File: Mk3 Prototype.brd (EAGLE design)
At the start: 113 x 55.2 mm, 176 parts, among them IC1 BD49XXX, IC2 CC3100, IC3 S25FL216K0PMFI011, IC4 STM32F401V, IC6 AP3419, J1 ZX62-AB-5PA(11), J2 SWD_SHROUD, J7 SFV30R-2STE1HLF, Q1 BSS84W, Q11 BSS84W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

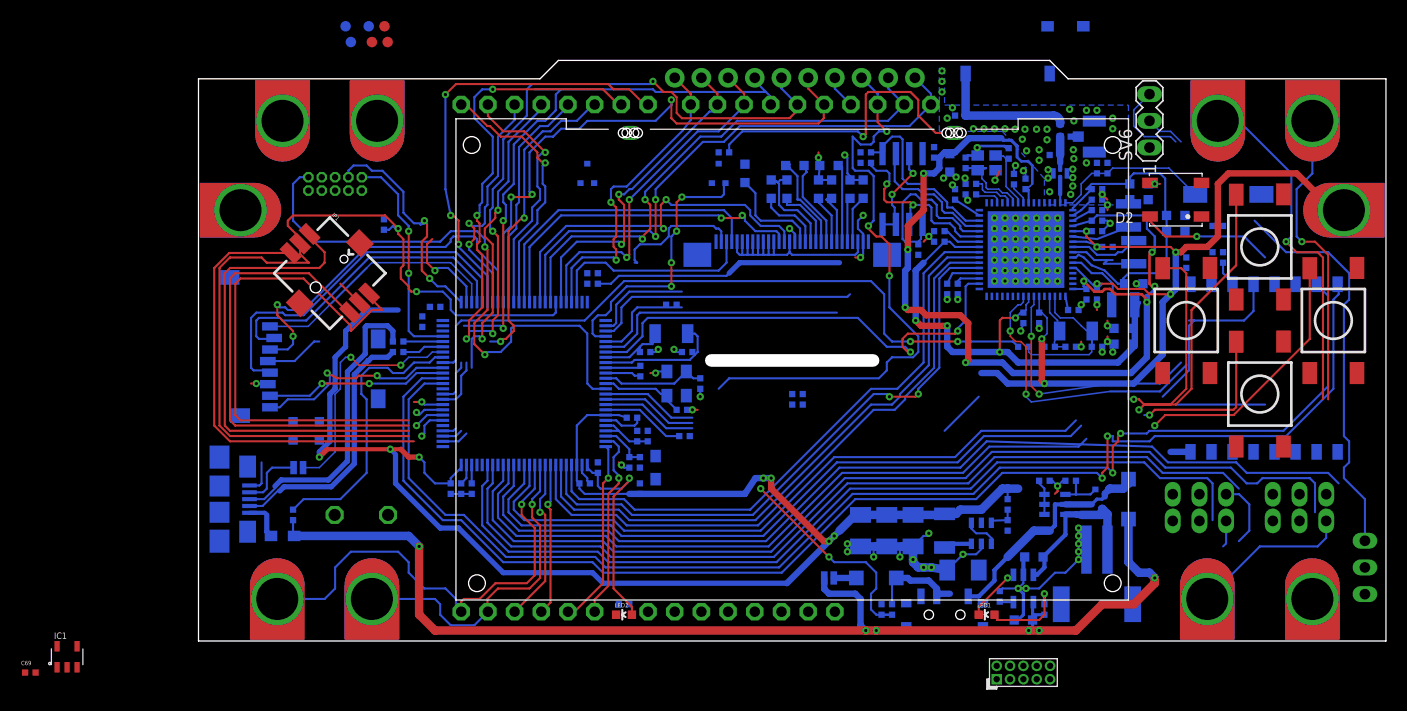
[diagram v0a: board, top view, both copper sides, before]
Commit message: added notes, increased via size
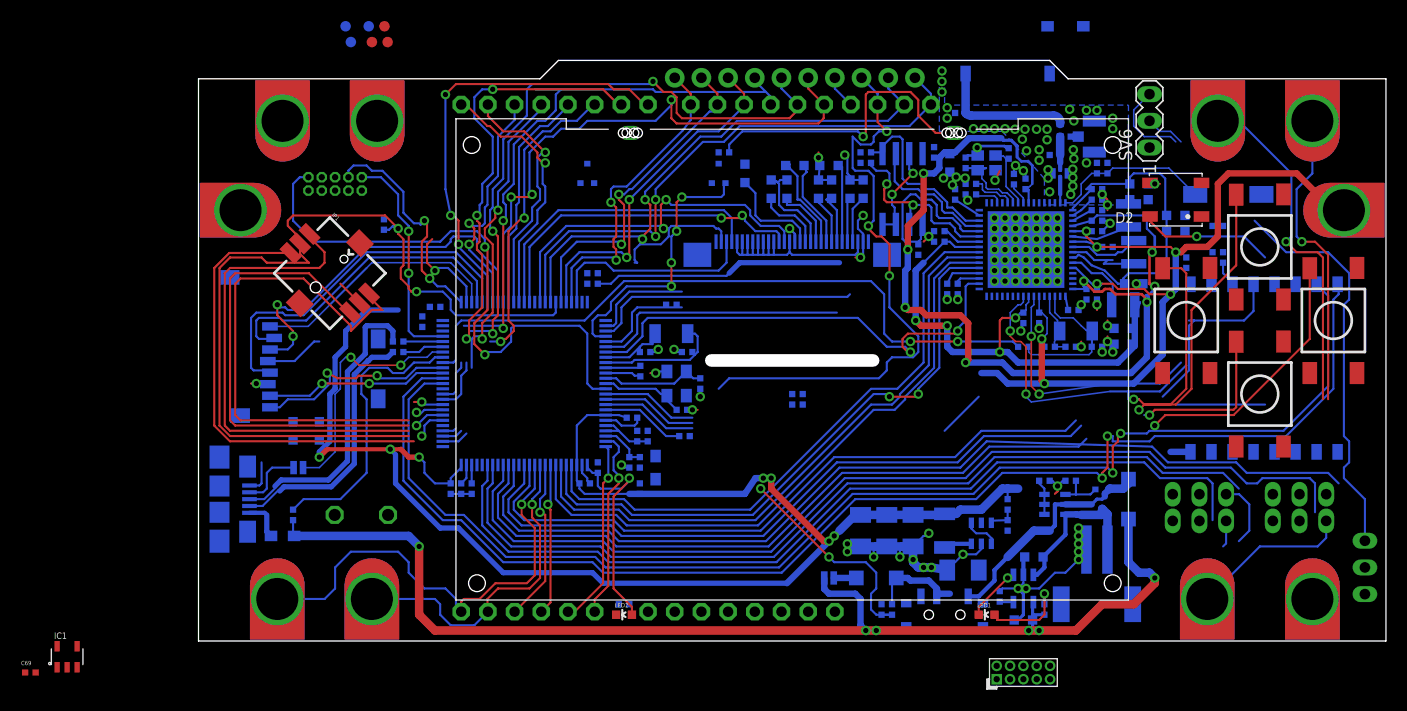
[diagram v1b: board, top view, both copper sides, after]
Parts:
- moved C2 0.25 mm to (72.5, 50.2)

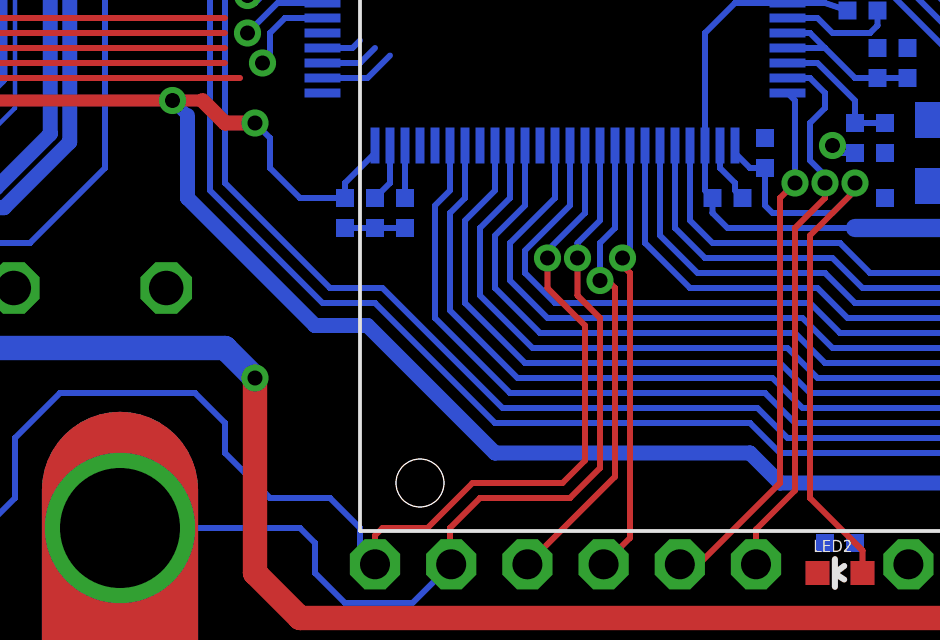
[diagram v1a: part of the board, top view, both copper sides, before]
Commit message: added two status leds
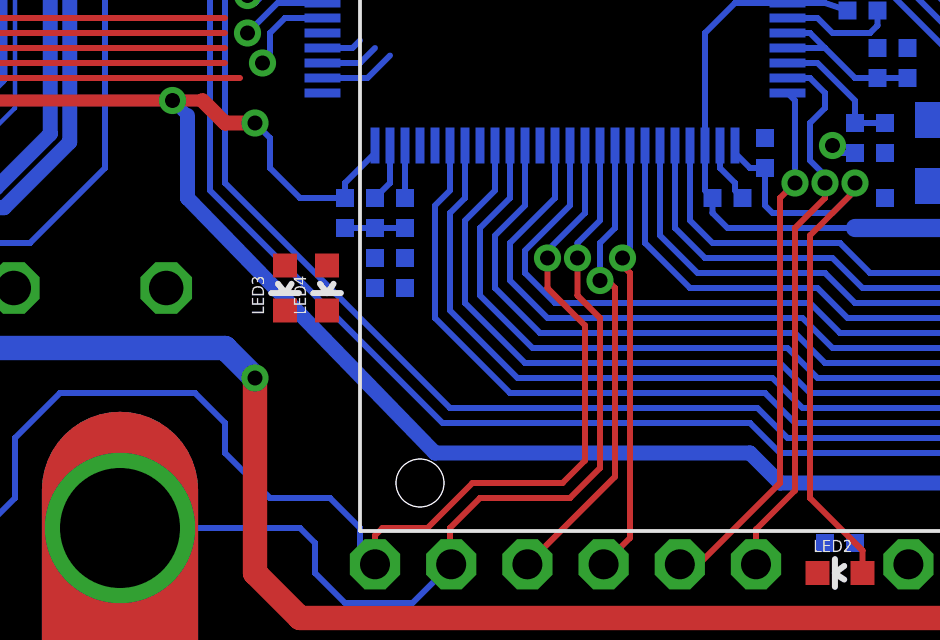
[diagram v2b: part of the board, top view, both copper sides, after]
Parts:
- added LED3, LED4: (no value), TiLDA Mk3 Parts:LED-0603-CORRECT
- added R34, R35: (no value), TiLDA Mk3 Parts:R0402-SMALLER
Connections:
- new net LED1: IC4.46, R34.2
- new net LED2: IC4.47, R35.2
- new net N$51: LED4.A, R35.1
- new net N$52: LED3.A, R34.1
- net GND: now also LED3.C, LED4.C
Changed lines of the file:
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@@
 <setting verticaltext="up"/>
 </settings>
-<grid distance="0.1" unitdist="mm" unit="mm" style="lines" multiple="1" display="yes" altdistance="0.25" altunitdist="mm" altunit="mm"/>
+<grid distance="0.5" unitdist="mm" unit="mm" style="lines" multiple="1" display="yes" altdistance="0.25" altunitdist="mm" altunit="mm"/>
 <layers>
 <layer number="1" name="Top" color="4" fill="1" visible="yes" active="yes"/>
@@
 <element name="IC1" library="TiLDA Mk3 Parts" package="SSOP5" value="BD49XXX" x="-12.5" y="-1.5"/>
 <element name="C69" library="TiLDA Mk3 Parts" package="C0402-SMALLER" value="0402/1n/10V/X5R" x="-16" y="-3"/>
+<element name="LED3" library="TiLDA Mk3 Parts" package="LED-0603-CORRECT" value="" x="22" y="12" rot="R90"/>
+<element name="LED4" library="TiLDA Mk3 Parts" package="LED-0603-CORRECT" value="" x="23.4" y="12" rot="R90"/>
+<element name="R34" library="TiLDA Mk3 Parts" package="R0402-SMALLER" value="" x="25.5" y="12" rot="MR180"/>
+<element name="R35" library="TiLDA Mk3 Parts" package="R0402-SMALLER" value="" x="25.5" y="13" rot="MR180"/>
 </elements>
 <signals>
@@
 <contactref element="IC1" pad="3"/>
 <contactref element="C69" pad="2"/>
+<contactref element="LED4" pad="C"/>
+<contactref element="LED3" pad="C"/>
 <wire x1="82.9" y1="50.6" x2="84.2" y2="58.5" width="0" layer="19" extent="16-16"/>
 <wire x1="81.35" y1="44.5" x2="82.65" y2="44.5" width="0" layer="19" extent="16-16"/>
@@
 <wire x1="56.5" y1="23.5" x2="47.75" y2="23.25" width="0" layer="19" extent="16-16"/>
 <wire x1="26" y1="14" x2="36.5" y2="16" width="0" layer="19" extent="16-16"/>
-<wire x1="18.04" y1="12" x2="24" y2="14" width="0" layer="19" extent="16-16"/>
+<wire x1="23.4" y1="11.25" x2="24" y2="14" width="0" layer="19" extent="1-16"/>
+<wire x1="22" y1="11.25" x2="23.4" y2="11.25" width="0" layer="19" extent="1-1"/>
+<wire x1="18.04" y1="12" x2="22" y2="11.25" width="0" layer="19" extent="1-1"/>
 <wire x1="12.96" y1="12" x2="18.04" y2="12" width="0" layer="19" extent="1-1"/>
 <wire x1="6" y1="15" x2="12.96" y2="12" width="0" layer="19" extent="16-16"/>
@@
 <via x="18.25" y="18.25" extent="1-16" drill="0.5" shape="octagon"/>
 <wire x1="18.75" y1="17.75" x2="18.75" y2="15" width="0.5" layer="16"/>
-<wire x1="18.75" y1="15" x2="23" y2="10.75" width="0.5" layer="16"/>
-<wire x1="23" y1="10.75" x2="24.75" y2="10.75" width="0.5" layer="16"/>
-<wire x1="24.75" y1="10.75" x2="29" y2="6.5" width="0.5" layer="16"/>
-<wire x1="29" y1="6.5" x2="37.5" y2="6.5" width="0.5" layer="16"/>
+<wire x1="18.75" y1="15" x2="27" y2="6.5" width="0.5" layer="16"/>
+<wire x1="27" y1="6.5" x2="37.5" y2="6.5" width="0.5" layer="16"/>
 <wire x1="37.5" y1="6.5" x2="38.5" y2="5.5" width="0.5" layer="16"/>
 <wire x1="38.5" y1="5.5" x2="56" y2="5.5" width="0.5" layer="16"/>
@@
 <wire x1="21.5" y1="24.5" x2="20" y2="23" width="0.2" layer="16"/>
 <wire x1="20" y1="23" x2="20" y2="15.5" width="0.2" layer="16"/>
-<wire x1="20" y1="15.5" x2="23.5" y2="12" width="0.2" layer="16"/>
-<wire x1="23.5" y1="12" x2="25.25" y2="12" width="0.2" layer="16"/>
-<wire x1="25.25" y1="12" x2="29.25" y2="8" width="0.2" layer="16"/>
-<wire x1="29.25" y1="8" x2="37.75" y2="8" width="0.2" layer="16"/>
+<wire x1="20" y1="15.5" x2="27.5" y2="8" width="0.2" layer="16"/>
+<wire x1="27.5" y1="8" x2="37.75" y2="8" width="0.2" layer="16"/>
 <wire x1="37.75" y1="8" x2="38.75" y2="7" width="0.2" layer="16"/>
 <wire x1="38.75" y1="7" x2="55.25" y2="7" width="0.2" layer="16"/>
@@
 <wire x1="21.25" y1="25" x2="19.5" y2="23.25" width="0.2" layer="16"/>
 <wire x1="19.5" y1="23.25" x2="19.5" y2="15.25" width="0.2" layer="16"/>
-<wire x1="19.5" y1="15.25" x2="23.25" y2="11.5" width="0.2" layer="16"/>
-<wire x1="23.25" y1="11.5" x2="25" y2="11.5" width="0.2" layer="16"/>
-<wire x1="25" y1="11.5" x2="29" y2="7.5" width="0.2" layer="16"/>
-<wire x1="29" y1="7.5" x2="37.5" y2="7.5" width="0.2" layer="16"/>
+<wire x1="19.5" y1="15.25" x2="27.25" y2="7.5" width="0.2" layer="16"/>
+<wire x1="27.25" y1="7.5" x2="37.5" y2="7.5" width="0.2" layer="16"/>
 <wire x1="74" y1="13.5" x2="62.5" y2="13.5" width="0.2" layer="16"/>
 <wire x1="62.5" y1="13.5" x2="55.5" y2="6.5" width="0.2" layer="16"/>
@@
 <contactref element="SV1" pad="2"/>
 </signal>
+<signal name="N$51">
+<contactref element="LED4" pad="A"/>
+<contactref element="R35" pad="1"/>
+<wire x1="25" y1="13" x2="23.4" y2="12.75" width="0" layer="19" extent="1-16"/>
+</signal>
+<signal name="N$52">
+<contactref element="LED3" pad="A"/>
+<contactref element="R34" pad="1"/>
+<wire x1="25" y1="12" x2="22" y2="12.75" width="0" layer="19" extent="1-16"/>
+</signal>
+<signal name="LED1">
+<contactref element="R34" pad="2"/>
+<contactref element="IC4" pad="46"/>
+<wire x1="26" y1="12" x2="27" y2="16.75" width="0" layer="19" extent="16-16"/>
+</signal>
+<signal name="LED2">
+<contactref element="R35" pad="2"/>
+<contactref element="IC4" pad="47"/>
+<wire x1="26" y1="13" x2="26.5" y2="16.75" width="0" layer="19" extent="16-16"/>
+</signal>
 </signals>

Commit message: power supply improvments
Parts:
- added D3: (no value), diode:SOD80C
- added F1: PTCSMD, SparkFun-PowerIC:PTC-1206
- added R36: 0402/47k/5%, TiLDA Mk3 Parts:R0402-SMALLER
- C37: value 0603/4u7u/10V/X5R -> 0603/4u7/10V/X5R
- C38: value (none) -> 0603/10u/16V/X5R; device TiLDA Mk3 Parts:C0603K-SMALL -> TiLDA Mk3 Parts:C0805K
- C58: value 22u -> 0603/10u/10V/X5R; device TiLDA Mk3 Parts:C1206K -> TiLDA Mk3 Parts:C0805K
- C59: value 22u -> 0402/4u7/10V/X5R; device TiLDA Mk3 Parts:C1206K -> TiLDA Mk3 Parts:C0402-SMALLER
- C60: value (none) -> 0603/1u/10V/X5R; device TiLDA Mk3 Parts:C1206K -> TiLDA Mk3 Parts:C0402-SMALLER
- C61: value 22u -> 0603/10u/16V/X5R; device TiLDA Mk3 Parts:C1206K -> TiLDA Mk3 Parts:C0805K
- C69: value 0402/1n/10V/X5R -> 0402/1n/10V/NP0
- R17: value (none) -> 0402/2k/5%
- R19, R20, R25, R26: value (none) -> 0402/220k/5%
- R22: value (none) -> 0402/2M2/5%
- moved C69 84.1 mm to (66.8, 12.0), flipped to the bottom, turned to 180 degrees
- moved IC1 76.0 mm to (62.8, 9.50), flipped to the bottom, turned to 180 degrees
- moved C60 21.0 mm to (43.0, 17.0), turned to 90 degrees
- moved R31 12.7 mm to (65.0, 8.75), turned to 90 degrees
- moved R32 12.0 mm to (65.0, 10.5), turned to 90 degrees
- moved C58 10.0 mm to (75.5, 9.50), turned to 90 degrees
- moved IC6 7.02 mm to (67.5, 9.75), turned to 180 degrees
- moved C59 6.26 mm to (62.5, 7.50), turned to 0 degrees
- moved C61 4.07 mm to (70.0, 9.75), turned to 90 degrees
- moved L5 2.92 mm to (46.0, 18.0), turned to 0 degrees
- moved G1 2.85 mm to (17.2, 14.2), turned to 270 degrees
- moved L6 2.00 mm to (8.00, 12.0)
- moved L7 1.80 mm to (72.5, 9.50), turned to 270 degrees
- moved R27 1.25 mm to (9.00, 13.2), turned to 0 degrees
- moved R34 0.79 mm to (26.2, 11.8), turned to 90 degrees
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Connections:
- new net N$55: F1.1, L6.2
- new net N$56: C59.1, IC1.2, R36.2
- net +3V3: no longer C59.1, C60.1
- net ADC_VBUS: now also C60.2
- net GND: now also C60.1, D3.A, U1.CD2; no longer C60.2
- net SDIO_SW: now also U1.CD1
- net VBUS: now also D3.C, F1.2; no longer L6.2
- net V_UNREG: now also R36.1; no longer IC1.2
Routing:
- net +3V3: track 286.0 -> 267.2 mm
- net VBUS: track 114.6 -> 98.3 mm, vias 6 -> 2
- net N$12: track 0.00 -> 6.91 mm
- net N$52: track 0.00 -> 5.02 mm, vias 0 -> 1
- net LED1: track 0.00 -> 4.96 mm
- net V_UNREG: track 12.6 -> 17.6 mm
- net LED2: track 0.00 -> 4.16 mm
- net N$56: track 0.00 -> 4.10 mm
- net N$26: track 2.64 -> 6.08 mm
- net N$55: track 0.00 -> 3.33 mm
- net GND: track 120.1 -> 123.4 mm, vias 138 -> 137
- net N$51: track 0.00 -> 2.52 mm, vias 0 -> 1
- net N$27: track 3.90 -> 2.13 mm
- net ADC_LIGHT: track 20.7 -> 21.9 mm
- net ADC_VIN: track 29.3 -> 30.1 mm
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
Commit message: bit of tidying up
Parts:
- removed D3: (no value), diode:SOD80C
- added R37: 0402/100K/5%, TiLDA Mk3 Parts:R0402-SMALLER
- R12, R13: value 0402/100K/5% -> 0402/220K/5%
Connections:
- net GND: now also R37.1; no longer D3.A
- net MOM_LEFT: now also R37.2
- net VBUS: no longer D3.C
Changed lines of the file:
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@@
 <element name="C32" library="TiLDA Mk3 Parts" package="C0402-SMALLER" value="0402/100n/10V/X5R" x="41.75" y="19.5" rot="MR270"/>
 <element name="C33" library="TiLDA Mk3 Parts" package="C0402-SMALLER" value="0402/100n/10V/X5R" x="42.75" y="19.5" rot="MR270"/>
-<element name="R12" library="TiLDA Mk3 Parts" package="R0402-SMALLER" value="0402/100K/5%" x="57" y="23.5" rot="MR0"/>
-<element name="R13" library="TiLDA Mk3 Parts" package="R0402-SMALLER" value="0402/100K/5%" x="57" y="22.5" rot="MR0"/>
+<element name="R12" library="TiLDA Mk3 Parts" package="R0402-SMALLER" value="0402/220K/5%" x="57" y="23.5" rot="MR0"/>
+<element name="R13" library="TiLDA Mk3 Parts" package="R0402-SMALLER" value="0402/220K/5%" x="57" y="22.5" rot="MR0"/>
 <element name="C34" library="TiLDA Mk3 Parts" package="C0402-SMALLER" value="0402/1u/10V/X5R" x="45" y="32" rot="MR0"/>
 <element name="R14" library="TiLDA Mk3 Parts" package="R0402-SMALLER" value="0402/100K/5%" x="17.646" y="39.636" rot="MR270"/>
@@
 <attribute name="PROD_ID" value="RES-11150" x="8.5" y="9.5" size="1.778" layer="28" rot="MR180" display="off"/>
 </element>
-<element name="D3" library="diode" package="SOD80C" value="" x="11.75" y="10" rot="MR90"/>
 <element name="C59" library="TiLDA Mk3 Parts" package="C0402-SMALLER" value="0402/4u7/10V/X5R" x="62.5" y="7.5" rot="MR0"/>
 <element name="R36" library="TiLDA Mk3 Parts" package="R0402-SMALLER" value="0402/47k/5%" x="64.5" y="7.5" rot="MR0"/>
 <element name="C60" library="TiLDA Mk3 Parts" package="C0402-SMALLER" value="0603/1u/10V/X5R" x="43" y="17" rot="MR90"/>
+<element name="R37" library="TiLDA Mk3 Parts" package="R0402-SMALLER" value="0402/100K/5%" x="-11.5" y="-3"/>
 </elements>
 <signals>
@@
 <wire x1="22.5" y1="12.75" x2="22" y2="12.75" width="0.2" layer="1"/>
 <wire x1="22.5" y1="14.25" x2="22.5" y2="12.75" width="0.2" layer="1"/>
-<contactref element="D3" pad="A"/>
 <contactref element="C59" pad="2"/>
 <contactref element="C60" pad="1"/>
@@
 <wire x1="74.75" y1="11.5" x2="74.75" y2="11.25" width="0.2" layer="16"/>
 <wire x1="74.75" y1="11.25" x2="75.5" y2="10.5" width="0.2" layer="16"/>
+<contactref element="R37" pad="1"/>
 <wire x1="82.9" y1="50.6" x2="84.2" y2="58.5" width="0" layer="19" extent="16-16"/>
 <wire x1="81.35" y1="44.5" x2="82.65" y2="44.5" width="0" layer="19" extent="16-16"/>
@@
 <wire x1="41.75" y1="20" x2="42.75" y2="20" width="0" layer="19" extent="16-16"/>
 <wire x1="41.5" y1="20.5" x2="41.75" y2="20" width="0" layer="19" extent="16-16"/>
-<wire x1="43" y1="16.5" x2="42.75" y2="20" width="0" layer="19" extent="16-16"/>
-<wire x1="41" y1="16.5" x2="43" y2="16.5" width="0" layer="19" extent="16-16"/>
+<wire x1="40" y1="17" x2="41.75" y2="20" width="0" layer="19" extent="1-16"/>
 <wire x1="42" y1="15" x2="41" y2="16.5" width="0" layer="19" extent="16-16"/>
+<wire x1="43" y1="16.5" x2="42" y2="15" width="0" layer="19" extent="16-16"/>
 <wire x1="38" y1="17" x2="40" y2="17" width="0" layer="19" extent="1-16"/>
 <wire x1="36.5" y1="16.75" x2="38" y2="17" width="0" layer="19" extent="16-16"/>
@@
 <wire x1="17.25" y1="11.71" x2="22" y2="12.75" width="0" layer="19" extent="1-1"/>
 <wire x1="17.25" y1="16.79" x2="17.25" y2="11.71" width="0" layer="19" extent="1-1"/>
-<wire x1="11.75" y1="11.7" x2="17.25" y2="11.71" width="0" layer="19" extent="16-16"/>
-<wire x1="6" y1="15" x2="11.75" y2="11.7" width="0" layer="19" extent="16-16"/>
-<wire x1="9" y1="20.875" x2="6" y2="17" width="0" layer="19" extent="16-16"/>
-<wire x1="11.5" y1="20.875" x2="9" y2="20.875" width="0" layer="19" extent="16-16"/>
+<wire x1="11.5" y1="20.875" x2="17.25" y2="16.79" width="0" layer="19" extent="16-16"/>
+<wire x1="9" y1="20.875" x2="11.5" y2="20.875" width="0" layer="19" extent="16-16"/>
 <wire x1="6.6" y1="24.44" x2="9" y2="20.875" width="0" layer="19" extent="16-16"/>
 <wire x1="3.95" y1="21.45" x2="5" y2="24.5" width="0" layer="19" extent="1-16"/>
+<wire x1="6" y1="17" x2="9" y2="20.875" width="0" layer="19" extent="16-16"/>
 <wire x1="17.1" y1="28.75" x2="11.5" y2="20.875" width="0" layer="19" extent="16-16"/>
 <wire x1="21.298" y1="30.888" x2="17.1" y2="28.75" width="0" layer="19" extent="16-16"/>
@@
 <wire x1="102.235" y1="11.43" x2="102.235" y2="13.97" width="0" layer="19" extent="1-1"/>
 <wire x1="111" y1="4.46" x2="102.235" y2="11.43" width="0" layer="19" extent="1-1"/>
+<wire x1="-12" y1="-3" x2="4.85" y2="14.8" width="0" layer="19" extent="1-16"/>
 </signal>
 <signal name="LCD_POWER">
@@
 <wire x1="74.5" y1="20" x2="82.5" y2="20" width="0.2" layer="16"/>
 <wire x1="82.5" y1="20" x2="83.5" y2="21" width="0.2" layer="16"/>
+<contactref element="R37" pad="2"/>
 <wire x1="83.5" y1="21" x2="89.5" y2="22" width="0" layer="19" extent="1-16"/>
+<wire x1="-11" y1="-3" x2="30" y2="12.5" width="0" layer="19" extent="1-16"/>
 </signal>
 <signal name="MOM_RIGHT">
@@
 <wire x1="80.5" y1="2.5" x2="79.375" y2="2.5" width="0.3048" layer="16"/>
 <contactref element="F1" pad="2"/>
-<contactref element="D3" pad="C"/>
 <wire x1="9.9" y1="9.5" x2="21" y2="9.5" width="1.27" layer="16"/>
 <wire x1="21" y1="9.5" x2="22.5" y2="8" width="1.27" layer="16"/>
@@
 <wire x1="88.5" y1="8.5" x2="88.5" y2="11.6" width="1.27" layer="16"/>
 <wire x1="86.5" y1="1" x2="80.5" y2="2.5" width="0" layer="19" extent="1-16"/>
-<wire x1="11.75" y1="8.3" x2="9.9" y2="9.5" width="0" layer="19" extent="16-16"/>
 <wire x1="8.5" y1="13.25" x2="9.9" y2="9.5" width="0" layer="19" extent="16-16"/>
 <wire x1="59.55" y1="6" x2="79.375" y2="3.6249" width="0" layer="19" extent="16-16"/>

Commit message: some routing tidying
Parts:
- moved R37 46.2 mm to (32.5, 11.2), flipped to the bottom
- moved D4 1.00 mm to (88.5, 12.5)
- moved C63 0.50 mm to (93.5, 36.0), turned to 0 degrees
- moved R23 0.50 mm to (98.0, 36.5)
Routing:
- net SPI4_MOSI: track 22.5 -> 94.5 mm, vias 1 -> 3
- net ESP_CH_PD: track 9.18 -> 71.0 mm, vias 0 -> 2
- net ESP_GPIO16: track 17.7 -> 70.8 mm, vias 0 -> 2
- net WIFI_INTR: track 12.4 -> 64.3 mm, vias 0 -> 2
- net ESP_GPIO0: track 31.3 -> 72.5 mm, vias 0 -> 2
- net N$47: track 31.5 -> 61.3 mm
- net MOM_UP: track 53.4 -> 83.0 mm, vias 1 -> 3
- net N$46: track 32.4 -> 60.3 mm
- net USART6_TX: track 121.9 -> 138.7 mm, vias 2 -> 0
- net USART6_RX: track 125.2 -> 141.4 mm, vias 2 -> 0
- net MOM_RIGHT: track 89.8 -> 104.3 mm
- net N$21: track 38.0 -> 50.1 mm, vias 0 -> 1
- net MOM_LEFT: track 82.3 -> 92.3 mm
- net TIM1_CH2: track 129.1 -> 137.4 mm, vias 1 -> 2
- net +3V3: track 267.2 -> 275.4 mm, vias 16 -> 18
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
